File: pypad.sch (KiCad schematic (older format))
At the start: 59 parts, among them J1 Conn_01x05_Male, K1 SW_SPST, K10 SW_SPST, K11 SW_SPST, K12 SW_SPST, K13 SW_SPST, K14 SW_SPST, K15 SW_SPST, K16 SW_SPST, K17 SW_SPST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

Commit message: Routing attempt number 2
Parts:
- D1, D10, D11, D12, D13, D14, D15, D16, D17, D18, D19, D2, D20, D3, D4, D5, D6, D7, D8, D9: footprint Diode_THT:D_DO-35_SOD27_P7.62mm_Horizontal -> PyPad_Footprints:D_DO-35_SOD27_P7.62mm_Horizontal
- K1, K10, K11, K12, K13, K14, K15, K16, K17, K18, K19, K2, K20, K3, K4, K5, K6, K7, K8, K9: footprint Button_Switch_Keyboard:SW_Cherry_MX_1.00u_PCB -> PyPad_Footprints:SW_Cherry_MX_1.00u_PCB
- R1, R10, R4, R7: value R -> 82
- R11, R2, R5, R8: value R -> 56
- R12, R3, R6, R9: value R -> 33
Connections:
- net PA8: now also R3.2; no longer R9.2
- net at U1.12 (PA3): now also R7.2; no longer R1.2
- net at U1.13 (PA2): now also R8.2; no longer R2.2
- net at U1.14 (PA1): now also R9.2; no longer R3.2
- net at U1.24 (PB9): now also R12.2; no longer R10.2
- net at U1.26 (PB7): now also R10.2; no longer R12.2
- net PB6: now reaches U1.27 (PB6)
- net PB6: now also R6.2; no longer R7.2
- net at U1.6 (PB1): now also R1.2; no longer R8.2
- net at U1.8 (PA7): now also R4.2; no longer R5.2
- net at U1.9 (PA6): now also R5.2; no longer R6.2
- net PB0: no longer names the net of U1.7 (PB0)
- net PB0: now also R2.2; no longer R4.2
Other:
- moved on the sheet: D1, D10, D11, D12, D13, D14, D15, D16, D17, D18, D19, D2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

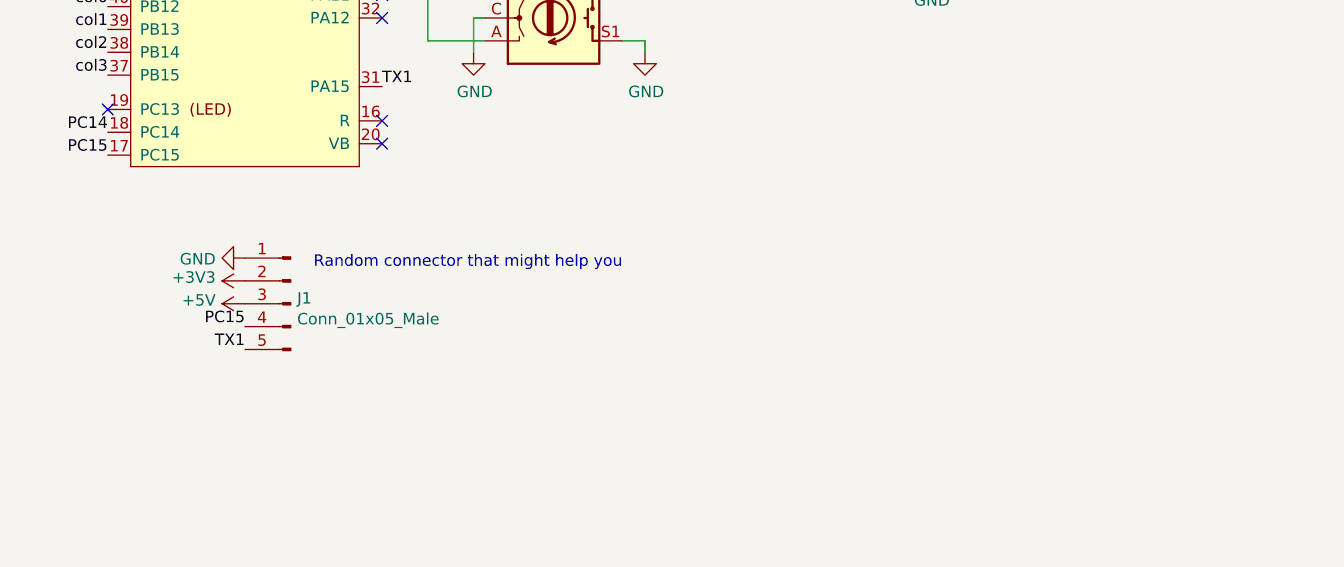
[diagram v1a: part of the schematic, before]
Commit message: Revision 2
Moved board around to allow M3 holes, rerouted using freeRouting and manually fixed.
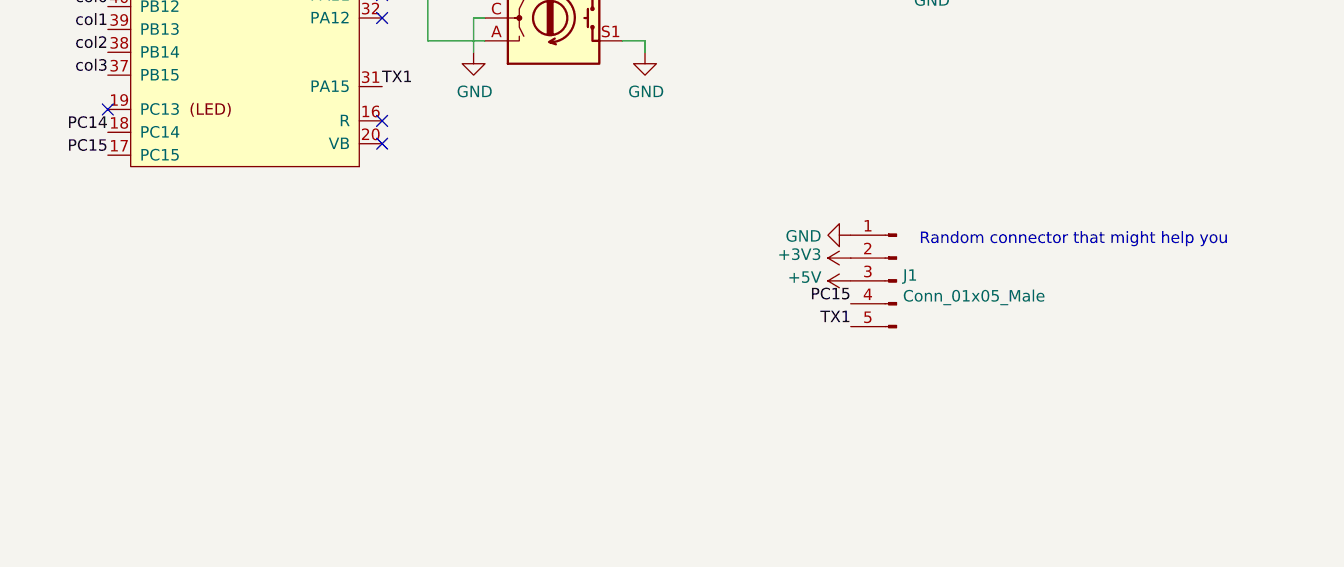
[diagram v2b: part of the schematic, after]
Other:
- moved on the sheet: J1
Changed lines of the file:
@@
 L Connector:Conn_01x05_Male J1
 U 1 1 5EFA0929
-P 6700 4200
-F 0 "J1" H 6672 4224 50  0000 R CNN
-F 1 "Conn_01x05_Male" H 6672 4133 50  0000 R CNN
-F 2 "Connector_PinHeader_2.54mm:PinHeader_1x05_P2.54mm_Vertical" H 6700 4200 50  0001 C CNN
-F 3 "~" H 6700 4200 50  0001 C CNN
-	1    6700 4200
+P 9350 4100
+F 0 "J1" H 9322 4124 50  0000 R CNN
+F 1 "Conn_01x05_Male" H 9322 4033 50  0000 R CNN
+F 2 "Connector_PinHeader_2.54mm:PinHeader_1x05_P2.54mm_Vertical" H 9350 4100 50  0001 C CNN
+F 3 "~" H 9350 4100 50  0001 C CNN
+	1    9350 4100
 	-1   0    0    -1
 $EndComp
@@
 L power:GND #PWR0109
 U 1 1 5EFA463B
-P 6500 4000
-F 0 "#PWR0109" H 6500 3750 50  0001 C CNN
-F 1 "GND" V 6505 3872 50  0000 R CNN
-F 2 "" H 6500 4000 50  0001 C CNN
-F 3 "" H 6500 4000 50  0001 C CNN
-	1    6500 4000
+P 9150 3900
+F 0 "#PWR0109" H 9150 3650 50  0001 C CNN
+F 1 "GND" V 9155 3772 50  0000 R CNN
+F 2 "" H 9150 3900 50  0001 C CNN
+F 3 "" H 9150 3900 50  0001 C CNN
+	1    9150 3900
 	0    1    1    0
 $EndComp
@@
 L power:+3V3 #PWR0110
 U 1 1 5EFA50C4
-P 6500 4100
-F 0 "#PWR0110" H 6500 3950 50  0001 C CNN
-F 1 "+3V3" V 6515 4228 50  0000 L CNN
-F 2 "" H 6500 4100 50  0001 C CNN
-F 3 "" H 6500 4100 50  0001 C CNN
-	1    6500 4100
+P 9150 4000
+F 0 "#PWR0110" H 9150 3850 50  0001 C CNN
+F 1 "+3V3" V 9165 4128 50  0000 L CNN
+F 2 "" H 9150 4000 50  0001 C CNN
+F 3 "" H 9150 4000 50  0001 C CNN
+	1    9150 4000
 	0    -1   -1   0
 $EndComp
@@
 L power:+5V #PWR0111
 U 1 1 5EFA5FC0
-P 6500 4200
-F 0 "#PWR0111" H 6500 4050 50  0001 C CNN
-F 1 "+5V" V 6515 4328 50  0000 L CNN
-F 2 "" H 6500 4200 50  0001 C CNN
-F 3 "" H 6500 4200 50  0001 C CNN
-	1    6500 4200
+P 9150 4100
+F 0 "#PWR0111" H 9150 3950 50  0001 C CNN
+F 1 "+5V" V 9165 4228 50  0000 L CNN
+F 2 "" H 9150 4100 50  0001 C CNN
+F 3 "" H 9150 4100 50  0001 C CNN
+	1    9150 4100
 	0    -1   -1   0
 $EndComp
-Text Label 6500 4300 2    50   ~ 0
+Text Label 9150 4200 2    50   ~ 0
 PC15
-Text Label 6500 4400 2    50   ~ 0
+Text Label 9150 4300 2    50   ~ 0
 TX1
-Text Notes 6800 4050 0    50   ~ 0
+Text Notes 9450 3950 0    50   ~ 0
 Random connector that might help you
 $Comp

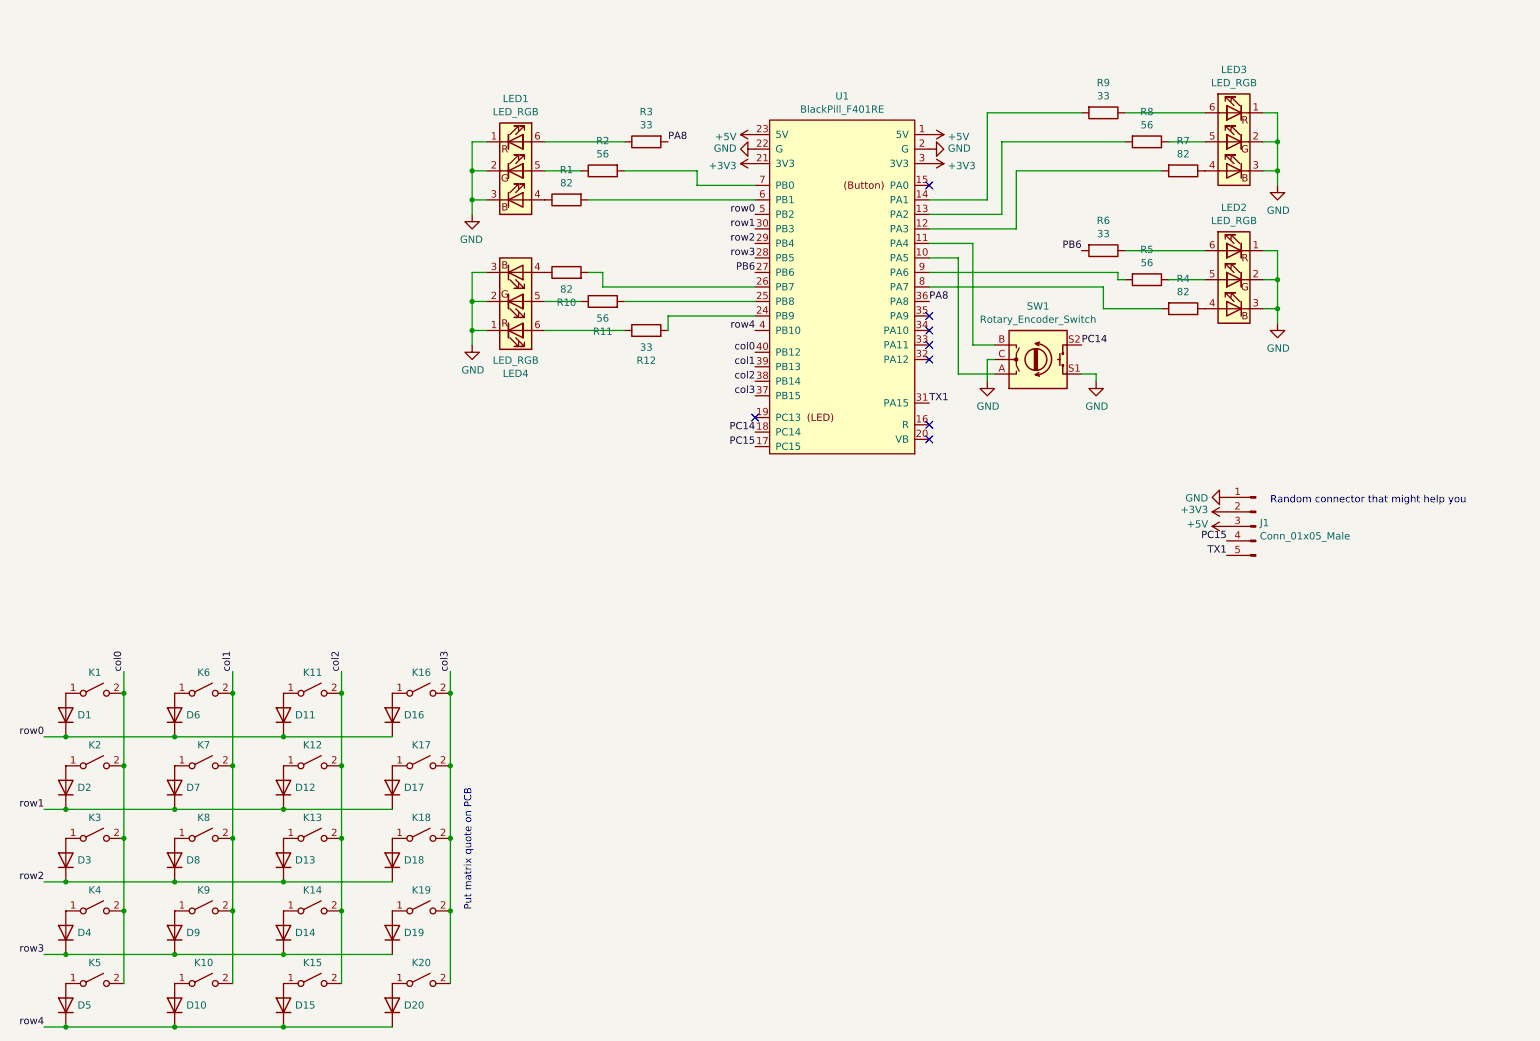
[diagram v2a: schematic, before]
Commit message: Added underglow RGB, misc tweaks
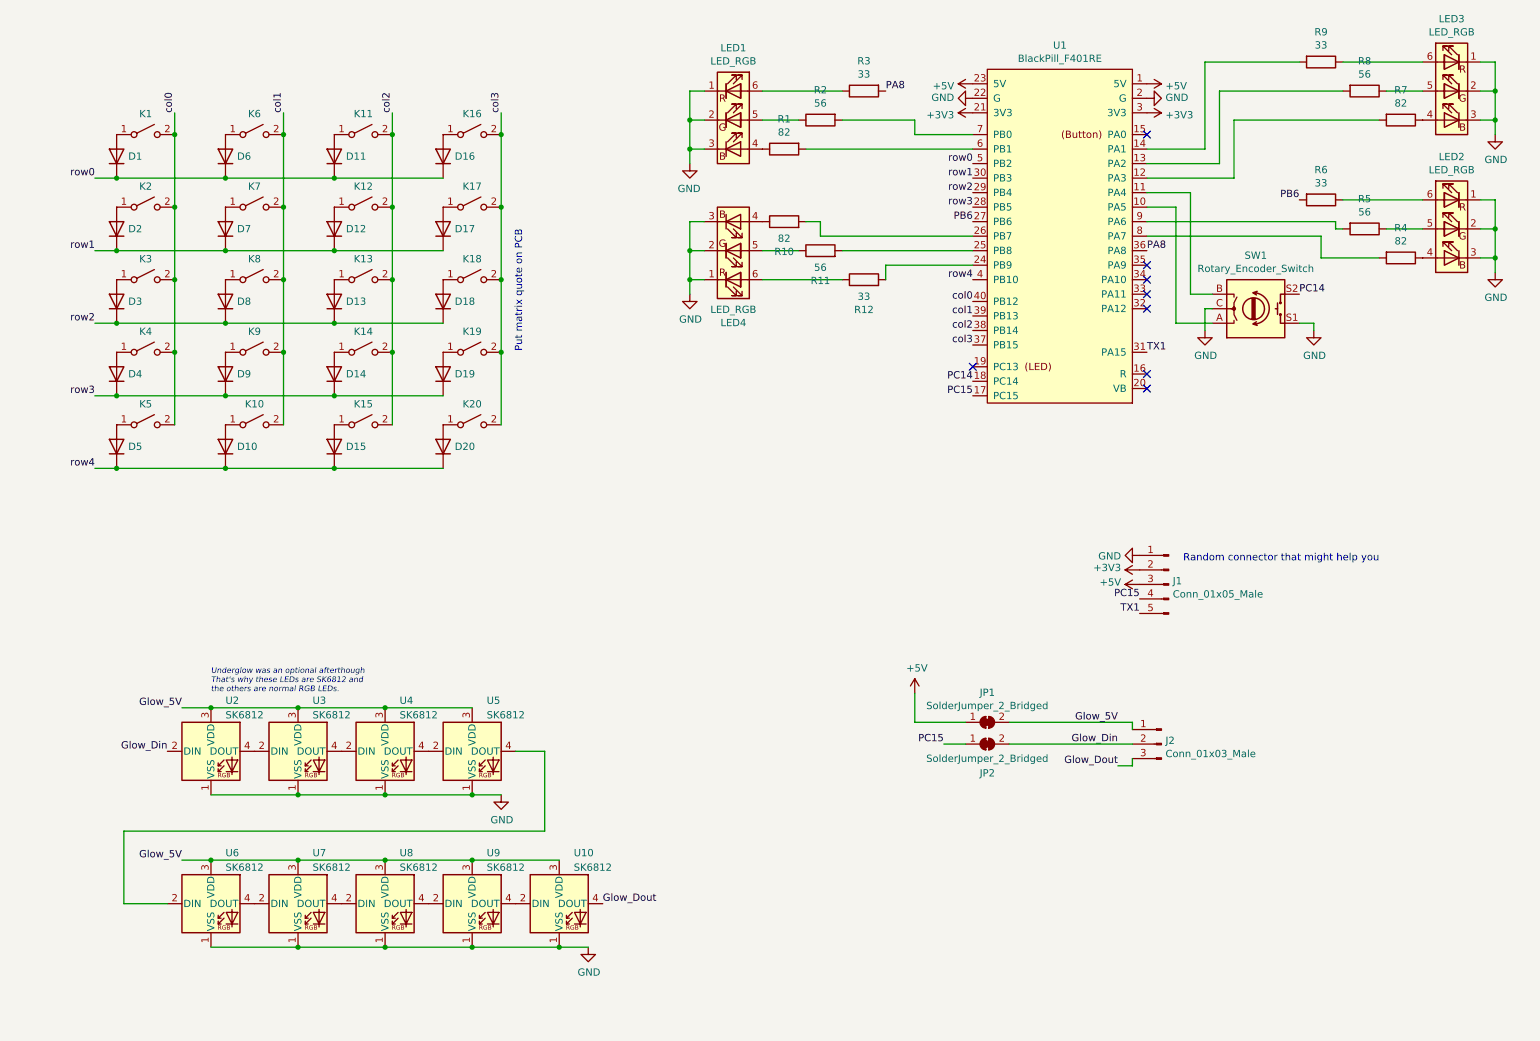
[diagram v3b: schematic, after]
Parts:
- added J2: Conn_01x03_Male, Connector_PinHeader_2.54mm:PinHeader_1x03_P2.54mm_Vertical, symbol Connector:Conn_01x03_Male
- added JP1, JP2: SolderJumper_2_Bridged, PyPad_Footprints:SolderJumper-2_P1.3mm_Bridged2BarCuttable_RoundedPad1.0x1.5mm, symbol Jumper:SolderJumper_2_Bridged
- added U10, U2, U3, U4, U5, U6, U7, U8, U9: SK6812, LED_SMD:LED_SK6812_PLCC4_5.0x5.0mm_P3.2mm, symbol LED:SK6812
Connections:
- net +5V: now also JP1.1 (A)
- net GND: now also U10.1 (VSS), U2.1 (VSS), U3.1 (VSS), U4.1 (VSS), U5.1 (VSS), U6.1 (VSS), U7.1 (VSS), U8.1 (VSS), U9.1 (VSS)
- net PC15: now also JP2.1 (A)
- new net: U2.4 (DOUT), U3.2 (DIN)
- new net: U3.4 (DOUT), U4.2 (DIN)
- new net: U4.4 (DOUT), U5.2 (DIN)
- new net: U5.4 (DOUT), U6.2 (DIN)
- new net: U6.4 (DOUT), U7.2 (DIN)
- new net: U7.4 (DOUT), U8.2 (DIN)
- new net: U8.4 (DOUT), U9.2 (DIN)
- new net: U10.2 (DIN), U9.4 (DOUT)
- new net Glow_5V: J2.1 (Pin_1), JP1.2 (B), U10.3 (VDD), U2.3 (VDD), U3.3 (VDD), U4.3 (VDD), U5.3 (VDD), U6.3 (VDD), U7.3 (VDD), U8.3 (VDD), U9.3 (VDD)
- new net Glow_Din: J2.2 (Pin_2), JP2.2 (B), U2.2 (DIN)
- new net Glow_Dout: J2.3 (Pin_3), U10.4 (DOUT)
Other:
- note added: "Underglow was an optional afterthough\nThat's why these LEDs are SK6812 and\nthe others are normal RGB LEDs."
- moved on the sheet: D1, D10, D11, D12, D13, D14, D15, D16, D17, D18, D19, D2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

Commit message: Revision 3
Added rotary encoder footprint, reorganised and rerouted board to accommodate.
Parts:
- SW1: footprint Rotary_Encoder:RotaryEncoder_Alps_EC11E-Switch_Vertical_H20mm -> PyPad_Footprints:RotaryEncoder_Bourns_PEC16-4-Switch_Vertical_H20mm
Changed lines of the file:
@@
 F 0 "SW1" H 9350 2233 50  0000 C CNN
 F 1 "Rotary_Encoder_Switch" H 9350 2324 50  0000 C CNN
-F 2 "Rotary_Encoder:RotaryEncoder_Alps_EC11E-Switch_Vertical_H20mm" H 9200 2760 50  0001 C CNN
+F 2 "PyPad_Footprints:RotaryEncoder_Bourns_PEC16-4-Switch_Vertical_H20mm" H 9200 2760 50  0001 C CNN
 F 3 "~" H 9350 2860 50  0001 C CNN
 	1    9350 2600
